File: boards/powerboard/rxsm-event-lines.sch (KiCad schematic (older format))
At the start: 9 parts, among them U601 PC3H7, U602 PC3H7, U603 PC3H7

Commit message: [powerboard] BLDC motor controller
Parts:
- R601, R602, R603, R604, R605, R606: footprint (none) -> Resistors_SMD:R_0603
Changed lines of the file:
@@
 LIBS:ds26lv32at
 LIBS:drv8312
+LIBS:drv8332
 LIBS:powerboard-cache
 EELAYER 25 0
@@
 F 0 "R605" V 6680 3200 50  0000 C CNN
 F 1 "3k" V 6600 3200 50  0000 C CNN
-F 2 "" V 6530 3200 50  0000 C CNN
+F 2 "Resistors_SMD:R_0603" V 6530 3200 50  0001 C CNN
 F 3 "" H 6600 3200 50  0000 C CNN
 	1    6600 3200
@@
 F 0 "R604" V 6480 3200 50  0000 C CNN
 F 1 "3k" V 6400 3200 50  0000 C CNN
-F 2 "" V 6330 3200 50  0000 C CNN
+F 2 "Resistors_SMD:R_0603" V 6330 3200 50  0001 C CNN
 F 3 "" H 6400 3200 50  0000 C CNN
 	1    6400 3200
@@
 F 0 "R606" V 6880 3200 50  0000 C CNN
 F 1 "3k" V 6800 3200 50  0000 C CNN
-F 2 "" V 6730 3200 50  0000 C CNN
+F 2 "Resistors_SMD:R_0603" V 6730 3200 50  0001 C CNN
 F 3 "" H 6800 3200 50  0000 C CNN
 	1    6800 3200
@@
 F 0 "R601" V 5380 3250 50  0000 C CNN
 F 1 "1k" V 5300 3250 50  0000 C CNN
-F 2 "" V 5230 3250 50  0000 C CNN
+F 2 "Resistors_SMD:R_0603" V 5230 3250 50  0001 C CNN
 F 3 "" H 5300 3250 50  0000 C CNN
 	1    5300 3250
@@
 F 0 "R602" V 5380 3700 50  0000 C CNN
 F 1 "1k" V 5300 3700 50  0000 C CNN
-F 2 "" V 5230 3700 50  0000 C CNN
+F 2 "Resistors_SMD:R_0603" V 5230 3700 50  0001 C CNN
 F 3 "" H 5300 3700 50  0000 C CNN
 	1    5300 3700
@@
 F 0 "R603" V 5380 4150 50  0000 C CNN
 F 1 "1k" V 5300 4150 50  0000 C CNN
-F 2 "" V 5230 4150 50  0000 C CNN
+F 2 "Resistors_SMD:R_0603" V 5230 4150 50  0001 C CNN
 F 3 "" H 5300 4150 50  0000 C CNN
 	1    5300 4150

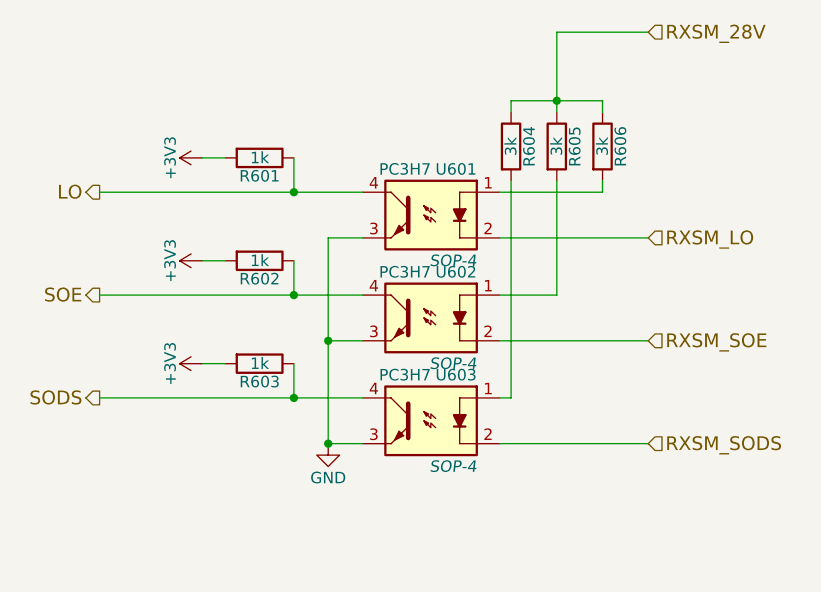
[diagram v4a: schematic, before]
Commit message: [powerboard] selected all components and assigned all footprints
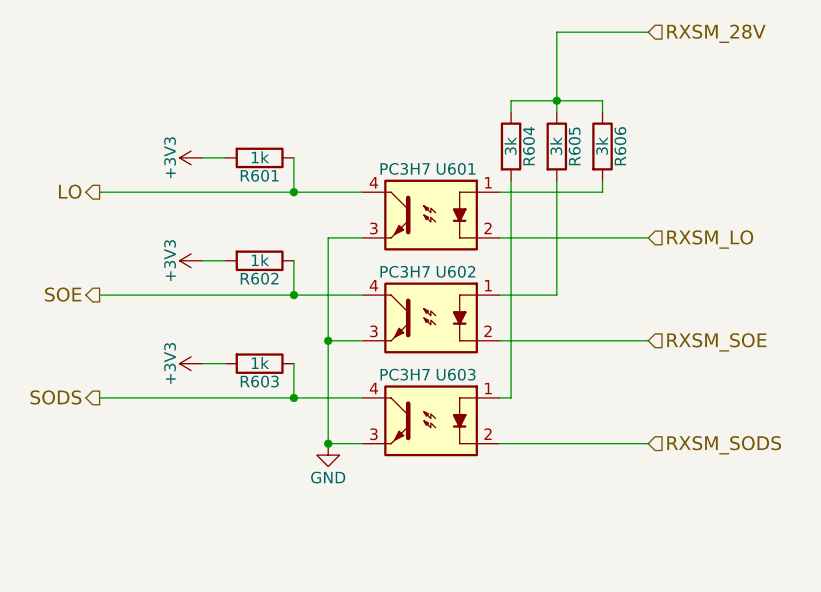
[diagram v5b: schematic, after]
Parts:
- U601, U602, U603: footprint SOP-4 -> SOP-4:SOP-4
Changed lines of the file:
@@
 F 0 "U601" H 5850 3700 50  0000 L CNN
 F 1 "PC3H7" H 6050 3700 50  0000 L CNN
-F 2 "SOP-4" H 5850 3300 50  0000 L CIN
+F 2 "SOP-4:SOP-4" H 5850 3300 50  0001 L CIN
 F 3 "" H 6075 3500 50  0000 L CNN
 	1    6050 3500
@@
 F 0 "U602" H 5850 4150 50  0000 L CNN
 F 1 "PC3H7" H 6050 4150 50  0000 L CNN
-F 2 "SOP-4" H 5850 3750 50  0000 L CIN
+F 2 "SOP-4:SOP-4" H 5850 3750 50  0001 L CIN
 F 3 "" H 6075 3950 50  0000 L CNN
 	1    6050 3950
@@
 F 0 "U603" H 5850 4600 50  0000 L CNN
 F 1 "PC3H7" H 6050 4600 50  0000 L CNN
-F 2 "SOP-4" H 5850 4200 50  0000 L CIN
+F 2 "SOP-4:SOP-4" H 5850 4200 50  0001 L CIN
 F 3 "" H 6075 4400 50  0000 L CNN
 	1    6050 4400
@@
 $EndComp
 $Comp
-L GND #PWR504
+L GND #PWR049
 U 1 1 5906A173
 P 5600 4500
-F 0 "#PWR504" H 5600 4250 50  0001 C CNN
+F 0 "#PWR049" H 5600 4250 50  0001 C CNN
 F 1 "GND" H 5600 4350 50  0000 C CNN
 F 2 "" H 5600 4500 50  0000 C CNN
@@
 $EndComp
 $Comp
-L +3V3 #PWR501
+L +3V3 #PWR050
 U 1 1 5906A180
 P 5050 3250
-F 0 "#PWR501" H 5050 3100 50  0001 C CNN
+F 0 "#PWR050" H 5050 3100 50  0001 C CNN
 F 1 "+3V3" H 5050 3390 50  0000 C CNN
 F 2 "" H 5050 3250 50  0000 C CNN
@@
 $EndComp
 $Comp
-L +3V3 #PWR502
+L +3V3 #PWR051
 U 1 1 5906A186
 P 5050 3700
-F 0 "#PWR502" H 5050 3550 50  0001 C CNN
+F 0 "#PWR051" H 5050 3550 50  0001 C CNN
 F 1 "+3V3" H 5050 3840 50  0000 C CNN
 F 2 "" H 5050 3700 50  0000 C CNN
@@
 $EndComp
 $Comp
-L +3V3 #PWR503
+L +3V3 #PWR052
 U 1 1 5906A19A
 P 5050 4150
-F 0 "#PWR503" H 5050 4000 50  0001 C CNN
+F 0 "#PWR052" H 5050 4000 50  0001 C CNN
 F 1 "+3V3" H 5050 4290 50  0000 C CNN
 F 2 "" H 5050 4150 50  0000 C CNN

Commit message: [powerboard] layout: parts placed; RS-422 termination added; various minor improvements
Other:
- note added: "From PDR Presentation "Power System""
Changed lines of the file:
@@
 $EndComp
 $Comp
-L GND #PWR049
+L GND #PWR051
 U 1 1 5906A173
 P 5600 4500
-F 0 "#PWR049" H 5600 4250 50  0001 C CNN
+F 0 "#PWR051" H 5600 4250 50  0001 C CNN
 F 1 "GND" H 5600 4350 50  0000 C CNN
 F 2 "" H 5600 4500 50  0000 C CNN
@@
 $EndComp
 $Comp
-L +3V3 #PWR050
+L +3V3 #PWR052
 U 1 1 5906A180
 P 5050 3250
-F 0 "#PWR050" H 5050 3100 50  0001 C CNN
+F 0 "#PWR052" H 5050 3100 50  0001 C CNN
 F 1 "+3V3" H 5050 3390 50  0000 C CNN
 F 2 "" H 5050 3250 50  0000 C CNN
@@
 $EndComp
 $Comp
-L +3V3 #PWR051
+L +3V3 #PWR053
 U 1 1 5906A186
 P 5050 3700
-F 0 "#PWR051" H 5050 3550 50  0001 C CNN
+F 0 "#PWR053" H 5050 3550 50  0001 C CNN
 F 1 "+3V3" H 5050 3840 50  0000 C CNN
 F 2 "" H 5050 3700 50  0000 C CNN
@@
 $EndComp
 $Comp
-L +3V3 #PWR052
+L +3V3 #PWR054
 U 1 1 5906A19A
 P 5050 4150
-F 0 "#PWR052" H 5050 4000 50  0001 C CNN
+F 0 "#PWR054" H 5050 4000 50  0001 C CNN
 F 1 "+3V3" H 5050 4290 50  0000 C CNN
 F 2 "" H 5050 4150 50  0000 C CNN
@@
 Text HLabel 7000 4500 2    60   Input ~ 0
 RXSM_SODS
+Text Notes 5350 5050 0    60   ~ 0
+From PDR Presentation "Power System"
 $EndSCHEMATC
